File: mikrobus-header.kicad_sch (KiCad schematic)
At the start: 5 parts, among them J3 Conn_01x08_Pin, J4 Conn_01x08_Pin, U5 TMP1827NGRR

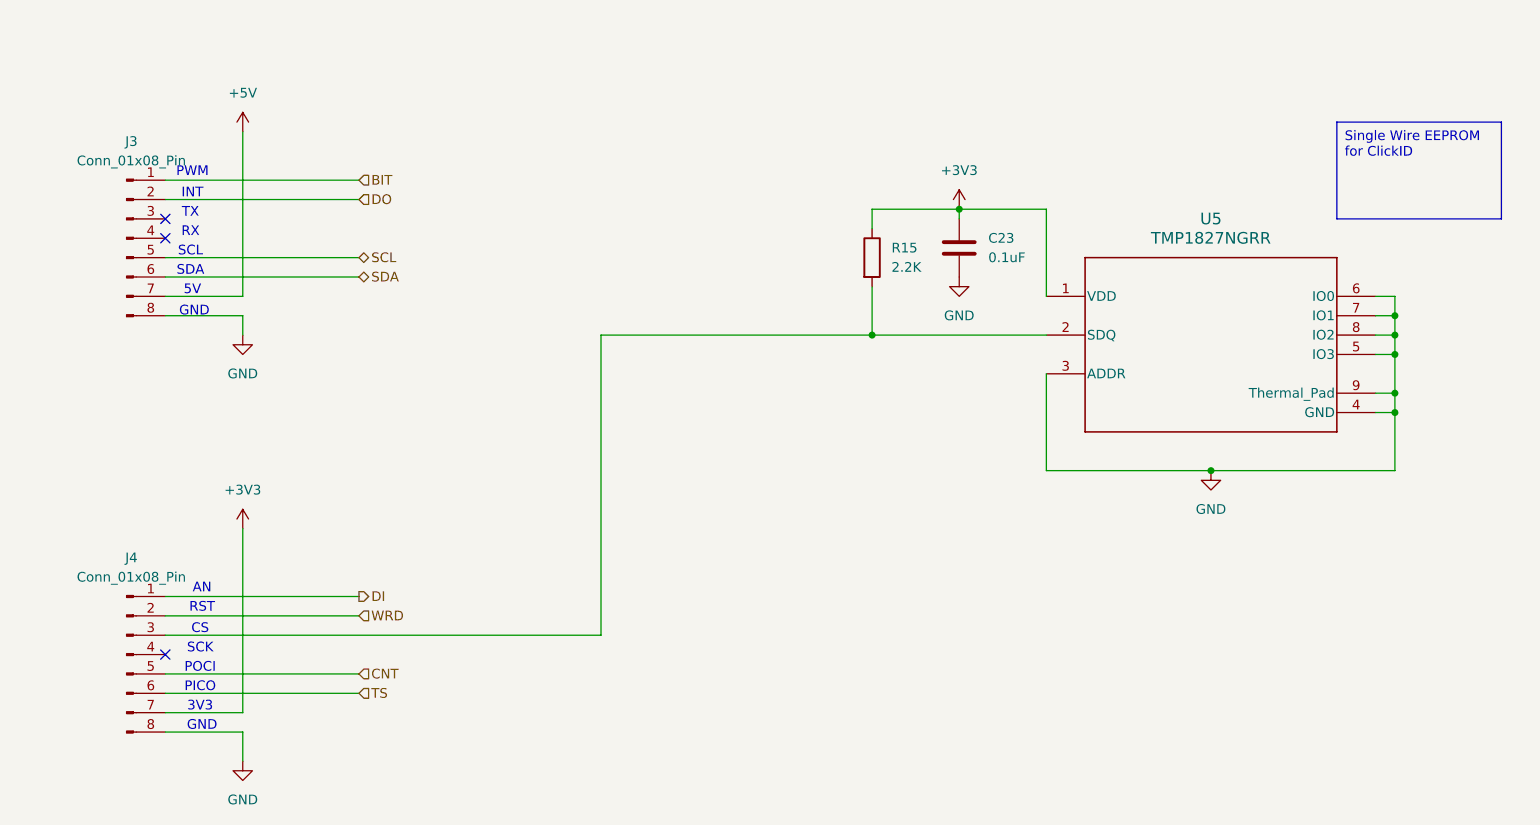
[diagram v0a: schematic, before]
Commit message: Resolved #7: swapped click board header connections and finished first pass routing
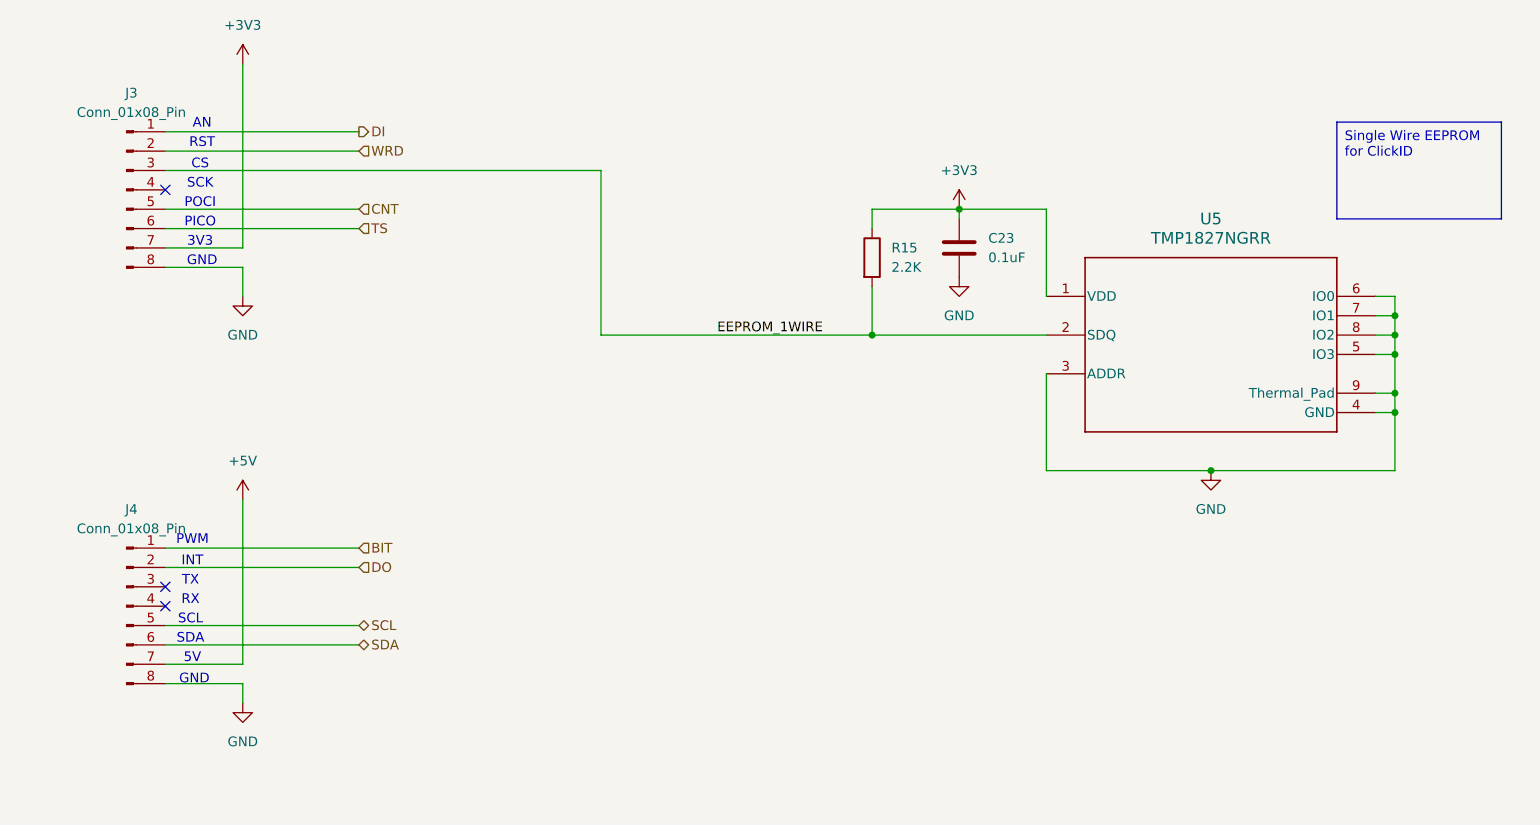
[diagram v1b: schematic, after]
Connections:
- net +3V3: now also J3.7 (Pin_7); no longer J4.7 (Pin_7)
- net +5V: now also J4.7 (Pin_7); no longer J3.7 (Pin_7)
- net BIT: now also J4.1 (Pin_1); no longer J3.1 (Pin_1)
- net CNT: now also J3.5 (Pin_5); no longer J4.5 (Pin_5)
- net DI: now also J3.1 (Pin_1); no longer J4.1 (Pin_1)
- net DO: now also J4.2 (Pin_2); no longer J3.2 (Pin_2)
- net SCL: now also J4.5 (Pin_5); no longer J3.5 (Pin_5)
- net SDA: now also J4.6 (Pin_6); no longer J3.6 (Pin_6)
- net TS: now also J3.6 (Pin_6); no longer J4.6 (Pin_6)
- net WRD: now also J3.2 (Pin_2); no longer J4.2 (Pin_2)
- net EEPROM_1WIRE: now reaches R15.2, U5.2 (SDQ)
- net EEPROM_1WIRE: now also J3.3 (Pin_3); no longer J4.3 (Pin_3)
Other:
- moved on the sheet: J3, J4

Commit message: Back-annotate BOM from CircuitHub
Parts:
- C23: MPN (none) -> CC0603KRX7R8BB104; Manufacturer (none) -> Yageo
- J3, J4: MPN (none) -> 2213S-08G; Manufacturer (none) -> Multicomp
- R15: MPN (none) -> CRCW060322K0JNEA; Manufacturer (none) -> Vishay
- U5: MPN (none) -> TMP1827NGRR; Manufacturer (none) -> Texas Instruments
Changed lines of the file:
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@@
+			)
+		)
+		(property "MPN" "2213S-08G"
+			(at 58.42 95.25 0)
+			(effects
+				(font
+					(size 1.27 1.27)
+				)
+				(hide yes)
+			)
+		)
+		(property "Manufacturer" "Multicomp"
+			(at 58.42 95.25 0)
+			(effects
+				(font
+					(size 1.27 1.27)
+				)
+				(hide yes)
 			)
 		)
@@
 			)
 		)
+		(property "MPN" "CRCW060322K0JNEA"
+			(at 156.21 49.53 0)
+			(effects
+				(font
+					(size 1.27 1.27)
+				)
+				(hide yes)
+			)
+		)
+		(property "Manufacturer" "Vishay"
+			(at 156.21 49.53 0)
+			(effects
+				(font
+					(size 1.27 1.27)
+				)
+				(hide yes)
+			)
+		)
 		(pin "2"
 		)
@@
 			)
 		)
+		(property "MPN" "2213S-08G"
+			(at 58.42 40.64 0)
+			(effects
+				(font
+					(size 1.27 1.27)
+				)
+				(hide yes)
+			)
+		)
+		(property "Manufacturer" "Multicomp"
+			(at 58.42 40.64 0)
+			(effects
+				(font
+					(size 1.27 1.27)
+				)
+				(hide yes)
+			)
+		)
 		(pin "7"
 		)
@@
 			)
 		)
+		(property "MPN" "TMP1827NGRR"
+			(at 179.07 54.61 0)
+			(effects
+				(font
+					(size 1.27 1.27)
+				)
+				(hide yes)
+			)
+		)
+		(property "Manufacturer" "Texas Instruments"
+			(at 179.07 54.61 0)
+			(effects
+				(font
+					(size 1.27 1.27)
+				)
+				(hide yes)
+			)
+		)
 		(pin "5"
 		)
@@
 			(at 167.64 48.26 0)
 			(effects
+				(font
+					(size 1.27 1.27)
+				)
+				(hide yes)
+			)
+		)
+		(property "MPN" "CC0603KRX7R8BB104"
+			(at 167.64 48.26 0)
+			(effects
+				(font
+					(size 1.27 1.27)
+				)
+				(hide yes)
+			)
+		)
+		(property "Manufacturer" "Yageo"
+			(at 167.64 48.26 0)
+			(effects

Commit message: remove TS
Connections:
- net TS: no longer names the net of J3.6 (Pin_6)
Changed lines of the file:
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@@
 (kicad_sch
-	(version 20231120)
+	(version 20250114)
 	(generator "eeschema")
-	(generator_version "8.0")
+	(generator_version "9.0")
 	(paper "USLetter")
 	(title_block
@@
 		(company "JKEmbedded, LLC")
 	)
+	(text "5V"
+		(exclude_from_sim no)
+		(at 67.056 102.108 0)
+		(effects
+			(font
+				(size 1.27 1.27)
+			)
+		)
+	)
+	(text "RST"
+		(exclude_from_sim no)
+		(at 68.326 34.544 0)
+		(effects
+			(font
+				(size 1.27 1.27)
+			)
+		)
+	)
+	(text "CS"
+		(exclude_from_sim no)
+		(at 68.072 37.338 0)
+		(effects
+			(font
+				(size 1.27 1.27)
+			)
+		)
+	)
+	(text "3V3"
+		(exclude_from_sim no)
+		(at 68.072 47.498 0)
+		(effects
+			(font
+				(size 1.27 1.27)
+			)
+		)
+	)
+	(text "SCK"
+		(exclude_from_sim no)
+		(at 68.072 39.878 0)
+		(effects
+			(font
+				(size 1.27 1.27)
+			)
+		)
+	)
+	(text "SDA"
+		(exclude_from_sim no)
+		(at 66.802 99.568 0)
+		(effects
+			(font
+				(size 1.27 1.27)
+			)
+		)
+	)
+	(text "GND"
+		(exclude_from_sim no)
+		(at 68.326 50.038 0)
+		(effects
+			(font
+				(size 1.27 1.27)
+			)
+		)
+	)
+	(text "AN"
+		(exclude_from_sim no)
+		(at 68.326 32.004 0)
+		(effects
+			(font
+				(size 1.27 1.27)
+			)
+		)
+	)
+	(text "SCL"
+		(exclude_from_sim no)
+		(at 66.802 97.028 0)
+		(effects
+			(font
+				(size 1.27 1.27)
+			)
+		)
+	)
+	(text "INT"
+		(exclude_from_sim no)
+		(at 67.056 89.408 0)
+		(effects
+			(font
+				(size 1.27 1.27)
+			)
+		)
+	)
+	(text "TX"
+		(exclude_from_sim no)
+		(at 66.802 91.948 0)
+		(effects
+			(font
+				(size 1.27 1.27)
+			)
+		)
+	)
+	(text "PWM"
+		(exclude_from_sim no)
+		(at 67.056 86.614 0)
+		(effects
+			(font
+				(size 1.27 1.27)
+			)
+		)
+	)
+	(text "GND"
+		(exclude_from_sim no)
+		(at 67.31 104.902 0)
+		(effects
+			(font
+				(size 1.27 1.27)
+			)
+		)
+	)
+	(text "PICO"
+		(exclude_from_sim no)
+		(at 68.072 44.958 0)
+		(effects
+			(font
+				(size 1.27 1.27)
+			)
+		)
+	)
+	(text "POCI"
+		(exclude_from_sim no)
+		(at 68.072 42.418 0)
+		(effects
+			(font
+				(size 1.27 1.27)
+			)
+		)
+	)
+	(text "RX"
+		(exclude_from_sim no)
+		(at 66.802 94.488 0)
+		(effects
+			(font
+				(size 1.27 1.27)
+			)
+		)
+	)
+	(text_box "Single Wire EEPROM for ClickID"
+		(exclude_from_sim no)
+		(at 217.17 31.75 0)
+		(size 21.59 12.7)
+		(margins 0.9525 0.9525 0.9525 0.9525)
+		(stroke
+			(width 0)
+			(type default)
+		)
+		(fill
+			(type none)
+		)
+		(effects
+			(font
+				(size 1.27 1.27)
+			)
+			(justify left top)
+		)
+	)
 	(junction
 		(at 156.21 59.69)
@@
 	(wire
 		(pts
-			(xy 63.5 45.72) (xy 88.9 45.72)
-		)
-		(stroke
-			(width 0)
-			(type default)
-		)
-	)
-	(wire
-		(pts
 			(xy 156.21 43.18) (xy 167.64 43.18)
 		)
@@
 			(width 0)
 			(type default)
-		)
-	)
-	(text_box "Single Wire EEPROM for ClickID"
-		(exclude_from_sim no)
-		(at 217.17 31.75 0)
-		(size 21.59 12.7)
-		(stroke
-			(width 0)
-			(type default)
-		)
-		(fill
-			(type none)
-		)
-		(effects
-			(font
-				(size 1.27 1.27)
-			)
-			(justify left top)
-		)
-	)
-	(text "5V"
-		(exclude_from_sim no)
-		(at 67.056 102.108 0)
-		(effects
-			(font
-				(size 1.27 1.27)
-			)
-		)
-	)
-	(text "RST"
-		(exclude_from_sim no)
-		(at 68.326 34.544 0)
-		(effects
-			(font
-				(size 1.27 1.27)
-			)
-		)
-	)
-	(text "CS"
-		(exclude_from_sim no)
-		(at 68.072 37.338 0)
-		(effects
-			(font
-				(size 1.27 1.27)
-			)
-		)
-	)
-	(text "3V3"
-		(exclude_from_sim no)
-		(at 68.072 47.498 0)
-		(effects
-			(font
-				(size 1.27 1.27)
-			)
-		)
-	)
-	(text "SCK"
-		(exclude_from_sim no)
-		(at 68.072 39.878 0)
-		(effects
-			(font
-				(size 1.27 1.27)
-			)
-		)
-	)
-	(text "SDA"
-		(exclude_from_sim no)
-		(at 66.802 99.568 0)
-		(effects
-			(font
-				(size 1.27 1.27)
-			)
-		)
-	)
-	(text "GND"
-		(exclude_from_sim no)
-		(at 68.326 50.038 0)
-		(effects
-			(font
-				(size 1.27 1.27)
-			)
-		)
-	)
-	(text "AN"
-		(exclude_from_sim no)
-		(at 68.326 32.004 0)
-		(effects
-			(font
-				(size 1.27 1.27)
-			)
-		)
-	)
-	(text "SCL"
-		(exclude_from_sim no)
-		(at 66.802 97.028 0)
-		(effects
-			(font
-				(size 1.27 1.27)
-			)
-		)
-	)
-	(text "INT"
-		(exclude_from_sim no)
-		(at 67.056 89.408 0)
-		(effects
-			(font
-				(size 1.27 1.27)
-			)
-		)
-	)
-	(text "TX"
-		(exclude_from_sim no)
-		(at 66.802 91.948 0)
-		(effects
-			(font
-				(size 1.27 1.27)
-			)
-		)
-	)
-	(text "PWM"
-		(exclude_from_sim no)
-		(at 67.056 86.614 0)
-		(effects
-			(font
-				(size 1.27 1.27)
-			)
-		)
-	)
-	(text "GND"
-		(exclude_from_sim no)
-		(at 67.31 104.902 0)
-		(effects
-			(font
-				(size 1.27 1.27)
-			)
-		)
-	)
-	(text "PICO"
-		(exclude_from_sim no)
-		(at 68.072 44.958 0)
-		(effects
-			(font
-				(size 1.27 1.27)
-			)
-		)
-	)
-	(text "POCI"
-		(exclude_from_sim no)
-		(at 68.072 42.418 0)
-		(effects
-			(font
-				(size 1.27 1.27)
-			)
-		)
-	)
-	(text "RX"
-		(exclude_from_sim no)
-		(at 66.802 94.488 0)
-		(effects
-			(font
-				(size 1.27 1.27)
-			)
 		)
 	)
@@
 		(effects
 			(font
-				(size 1.27 1.27)
-			)
-			(justify left)
-		)
-	)
-	(hierarchical_label "TS"
-		(shape input)
-		(at 88.9 45.72 0)
-		(effects
-			(font

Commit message: Working through DRCs
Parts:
- J3: value Conn_01x08_Pin -> MIKRO_LEFT; footprint Connector_PinHeader_2.54mm:PinHeader_1x08_P2.54mm_Vertical -> Library:MIKROBUS_CLICK_LEFT_1x08_P2.54mm_Vertical
- J4: value Conn_01x08_Pin -> MIKRO_RIGHT; footprint Connector_PinHeader_2.54mm:PinHeader_1x08_P2.54mm_Vertical -> Library:MIKROBUS_CLICK_RIGHT_1x08_P2.54mm_Vertical; symbol Connector:Conn_01x08_Pin -> Library:MIKRO_RIGHT_01x08_Pin
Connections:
- net +5V: now also J4.10 (Pin_10); no longer J4.7 (Pin_7)
- net BIT: now also J4.16 (Pin_16); no longer J4.1 (Pin_1)
- net DO: now also J4.15 (Pin_15); no longer J4.2 (Pin_2)
- net GND: now also J4.9 (Pin_9); no longer J4.8 (Pin_8)
- net SCL: now also J4.12 (Pin_12); no longer J4.5 (Pin_5)
- net SDA: now also J4.11 (Pin_11); no longer J4.6 (Pin_6)
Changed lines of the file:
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@@
 	)
 	(symbol
-		(lib_id "Connector:Conn_01x08_Pin")
+		(lib_id "Library:MIKRO_RIGHT_01x08_Pin")
 		(at 58.42 95.25 0)
 		(unit 1)
@@
 			)
 		)
-		(property "Value" "Conn_01x08_Pin"
+		(property "Value" "MIKRO_RIGHT"
 			(at 59.055 85.09 0)
 			(effects
@@
 			)
 		)
-		(property "Footprint" "Connector_PinHeader_2.54mm:PinHeader_1x08_P2.54mm_Vertical"
+		(property "Footprint" "Library:MIKROBUS_CLICK_RIGHT_1x08_P2.54mm_Vertical"
 			(at 58.42 95.25 0)
 			(effects
@@
 			)
 		)
-		(pin "7"
-		)
-		(pin "2"
-		)
-		(pin "1"
-		)
-		(pin "4"
-		)
-		(pin "5"
-		)
-		(pin "8"
-		)
-		(pin "6"
-		)
-		(pin "3"
+		(pin "11"
+		)
+		(pin "16"
+		)
+		(pin "14"
+		)
+		(pin "9"
+		)
+		(pin "15"
+		)
+		(pin "10"
+		)
+		(pin "12"
+		)
+		(pin "13"
 		)
 		(instances
@@
 			)
 		)
-		(property "Value" "Conn_01x08_Pin"
+		(property "Value" "MIKRO_LEFT"
 			(at 59.055 30.48 0)
 			(effects
@@
 			)
 		)
-		(property "Footprint" "Connector_PinHeader_2.54mm:PinHeader_1x08_P2.54mm_Vertical"
+		(property "Footprint" "Library:MIKROBUS_CLICK_LEFT_1x08_P2.54mm_Vertical"
 			(at 58.42 40.64 0)
 			(effects

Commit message: Changed codec rail to 3V3_Osc and addressed all DRCs (including previous overrides)
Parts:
- U5: footprint Library:NGR0008B-IPC_A -> Package_SON:WSON-8-1EP_3x2.5mm_P0.5mm_EP1.2x1.5mm_PullBack_ThermalVias
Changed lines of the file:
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@@
 		(on_board yes)
 		(dnp no)
-		(fields_autoplaced yes)
 		(property "Reference" "J3"
-			(at 59.055 27.94 0)
+			(at 57.15 40.6399 0)
 			(effects
 				(font
 					(size 1.27 1.27)
 				)
+				(justify right)
 			)
 		)
 		(property "Value" "MIKRO_LEFT"
-			(at 59.055 30.48 0)
+			(at 57.15 43.1799 0)
 			(effects
 				(font
 					(size 1.27 1.27)
 				)
+				(justify right)
 			)
 		)
@@
 			)
 		)
-		(property "Footprint" "Library:NGR0008B-IPC_A"
+		(property "Footprint" "Package_SON:WSON-8-1EP_3x2.5mm_P0.5mm_EP1.2x1.5mm_PullBack_ThermalVias"
 			(at 179.07 54.61 0)
 			(effects
